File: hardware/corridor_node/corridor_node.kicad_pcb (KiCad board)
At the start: 2 copper layers, 40 x 40 mm, 47 parts, among them J1 Screw_Terminal_01x06, J2 Screw_Terminal_01x04, J3 RDB223, U1 SD3361, U2 SD3361, U3 LMV321, U4 TTY020-CA6, U5 AP7384-50SA

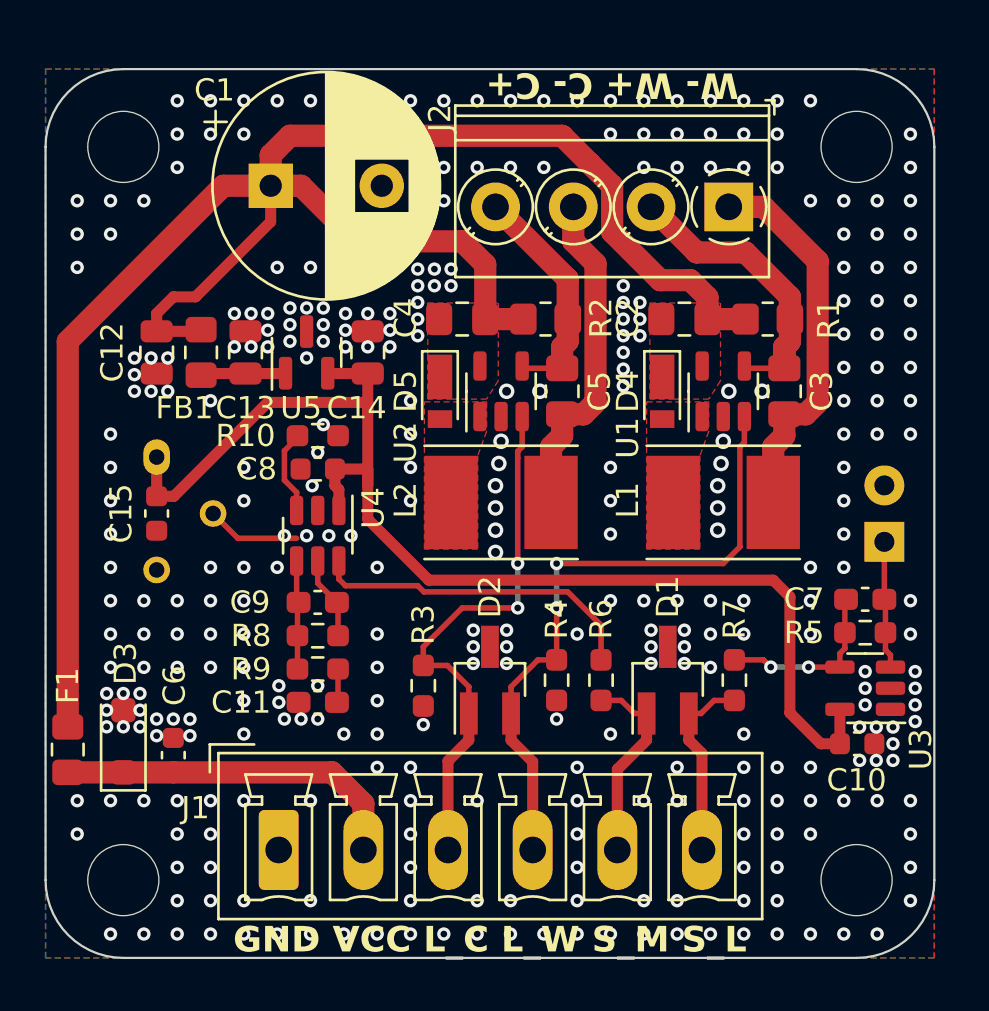
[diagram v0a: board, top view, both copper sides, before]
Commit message: led balance and corridor ready
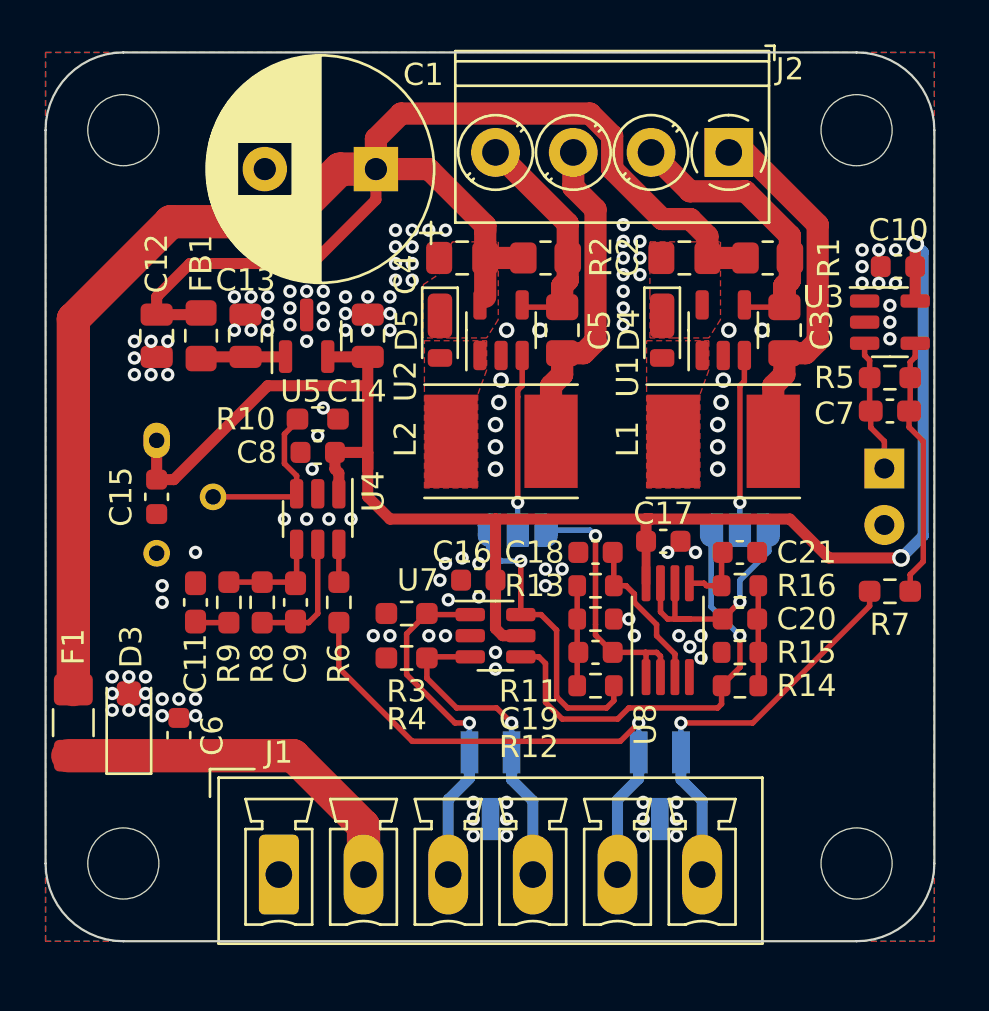
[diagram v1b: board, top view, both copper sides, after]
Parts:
- added C16: 100n 50V, Capacitor_SMD:C_0603_1608Metric, F.Cu at (144.5, 91.2)
- added C17: 100n 50V, Capacitor_SMD:C_0603_1608Metric, F.Cu at (152.8, 89.5)
- added C18: 100n 50V, Capacitor_SMD:C_0603_1608Metric, F.Cu at (149.8, 90.0)
- added C19: 100n 50V, Capacitor_SMD:C_0603_1608Metric, F.Cu at (149.8, 94.5)
- added C20: 100n 50V, Capacitor_SMD:C_0603_1608Metric, F.Cu at (156.2, 93.0)
- added C21: 100n 50V, Capacitor_SMD:C_0603_1608Metric, F.Cu at (156.2, 90.0)
- added JP1: SolderJumper_3_Open, Jumper:SolderJumper-3_P1.3mm_Open_RoundedPad1.0x1.5mm_NumberLabels, B.Cu at (146.2, 89.0)
- added JP2: SolderJumper_3_Open, Jumper:SolderJumper-3_P1.3mm_Open_RoundedPad1.0x1.5mm_NumberLabels, B.Cu at (156.2, 89.0)
- added R11: 100k, Resistor_SMD:R_0603_1608Metric, F.Cu at (149.8, 93.0)
- added R12: 100k, Resistor_SMD:R_0603_1608Metric, F.Cu at (149.8, 96.0)
- added R13: 100k, Resistor_SMD:R_0603_1608Metric, F.Cu at (149.8, 91.5)
- added R14: 100k, Resistor_SMD:R_0603_1608Metric, F.Cu at (156.2, 96.0)
- added R15: 100k, Resistor_SMD:R_0603_1608Metric, F.Cu at (156.2, 94.5)
- added R16: 100k, Resistor_SMD:R_0603_1608Metric, F.Cu at (156.2, 91.5)
- added U7: 74LVC2G17, Package_TO_SOT_SMD:SOT-23-6, F.Cu at (145.2, 93.8)
- added U8: LMV358, Package_SO:MSOP-8_3x3mm_P0.65mm, F.Cu at (153.0, 93.5)
- C1: value C_Polarized -> 470uF 50V
- C10, C15, C7, C8: value C -> 100n 50V
- C11: value C -> 10u 16V
- C12, C13, C2, C3, C4, C5: value C -> 10u 50V
- C14: value C -> 22u 10V
- C6: value C -> 1n 1kV
- C9: value 100n -> 100n 50V
- D1, D2: value D -> SM05; moved to B.Cu
- D3: value D_Zener -> SMF36A
- D4, D5: value D_Schottky -> RB160VA-40TR
- D6: value D_Photo -> TEPT5700
- F1: value Fuse -> 500mA; footprint Fuse:Fuse_0805_2012Metric_Pad1.15x1.40mm_HandSolder -> Fuse:Fuse_1206_3216Metric_Pad1.42x1.75mm_HandSolder
- FB1: value FerriteBead -> MMZ2012R102AT000
- L1, L2: value L -> 100uH
- R1, R2: value R -> 0.4
- R10: value R -> 47k
- R3, R4: value R -> 1k
- R5: value R -> 1M
- R6, R7: value R -> 100
- R9: value R -> 10k
- U6: renamed from J3; value RDB223 -> PIR
- moved C10 21.6 mm to (163.4, 77.1), turned to 180 degrees
- moved U3 16.5 mm to (163.0, 79.6), turned to 0 degrees
- moved R6 12.3 mm to (138.2, 92.2)
- moved R5 11.5 mm to (163.0, 82.1), turned to 0 degrees
- moved C7 8.55 mm to (163.0, 83.6), turned to 0 degrees
- moved R7 8.06 mm to (163.0, 91.8), turned to 0 degrees
- moved C11 7.11 mm to (131.7, 92.2), turned to -90 degrees
- moved R4 6.82 mm to (141.2, 94.8), turned to 0 degrees
- moved R9 5.00 mm to (133.2, 92.2), turned to -90 degrees
- moved C1 4.79 mm to (139.9, 72.7), turned to 180 degrees
- moved D1 4.76 mm to (152.6, 100.5), turned to -90 degrees
- moved D2 4.75 mm to (145.0, 100.5), turned to -90 degrees
- moved R3 3.34 mm to (141.2, 92.8), turned to 0 degrees
- moved D6 3.30 mm to (162.8, 86.2), turned to -90 degrees
- moved R8 2.92 mm to (134.7, 92.2), turned to -90 degrees
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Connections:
- U1 pad 3: /LED_W -> /PWM to DC/OUT1
- U2 pad 3: /LED_C -> /PWM to DC/OUT0
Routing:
- net +5V: track 56.1 -> 77.5 mm, vias 0 -> 2
- net /PWM to DC/PWM1: track 0.00 -> 20.2 mm, vias 0 -> 1
- net /SEN_M: track 8.98 -> 24.5 mm, vias 0 -> 1
- net /LED_W: track 29.1 -> 14.7 mm, vias 2 -> 1
- net /PWM to DC/PWM0: track 0.00 -> 13.4 mm, vias 0 -> 1
- net /sensors/PIR: track 15.0 -> 1.70 mm
- net Net-(JP1-B): track 0.00 -> 12.2 mm, vias 0 -> 1
- net Net-(JP2-B): track 0.00 -> 11.4 mm, vias 0 -> 1
- net /SEN_L: track 8.68 -> 18.6 mm, vias 0 -> 1
- net /LED_C: track 24.7 -> 16.0 mm, vias 2 -> 1
- net /PWM to DC/OUT1: track 0.00 -> 7.95 mm, vias 0 -> 1
- net /PWM to DC/OUT0: track 0.00 -> 7.95 mm, vias 0 -> 1
- net /PWM to DC/PWM0B: track 0.00 -> 7.09 mm
- net /PWM to DC/PWM0A: track 0.00 -> 4.54 mm
- net /PWM to DC/PWM1A: track 0.00 -> 4.54 mm
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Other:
- board text added: "1=PWM 3=DCV"
